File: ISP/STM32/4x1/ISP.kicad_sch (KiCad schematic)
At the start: 1 part

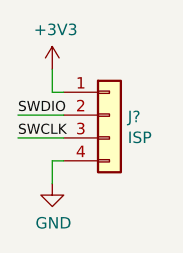
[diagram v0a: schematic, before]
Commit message: Fix grid alignment and update to KiCad 9
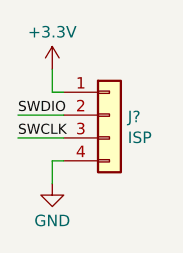
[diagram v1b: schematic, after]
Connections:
- net +3V3 renamed +3.3V
